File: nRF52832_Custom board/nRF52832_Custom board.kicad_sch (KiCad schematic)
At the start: 46 parts, among them J1 USB_C, J2 Battery Connector, J3 Analog, J4 PO PINS, J5 PO PINS, J6 PO PINS, J7 POWER, J8 GND, J9 Programming, SW1 SW_Push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

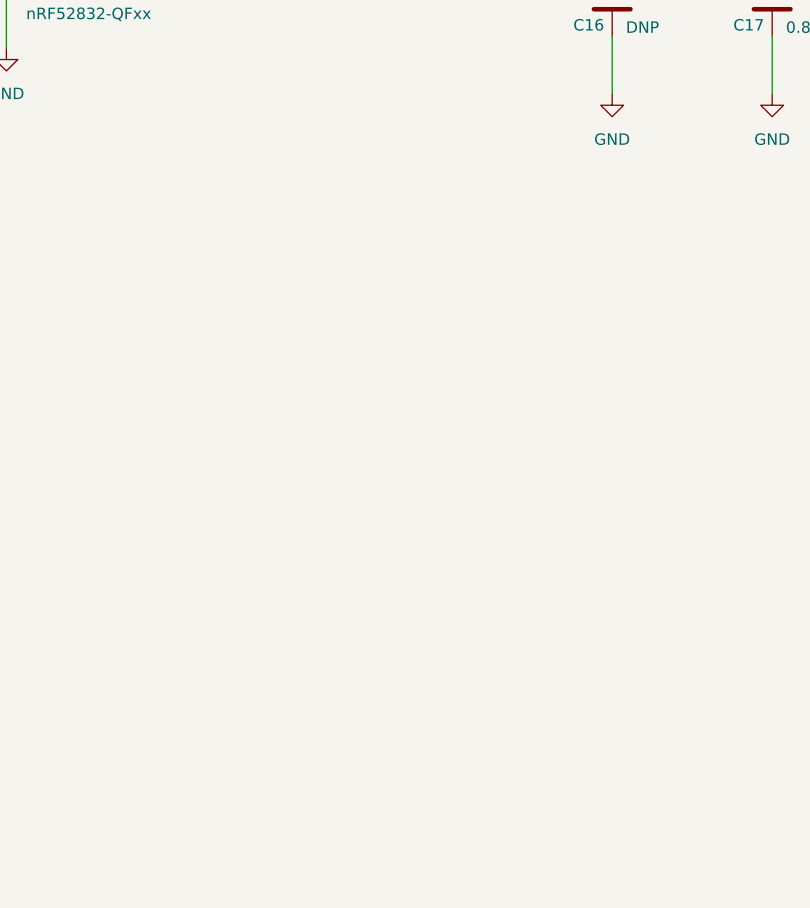
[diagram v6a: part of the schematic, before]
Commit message: update i2C and SPI
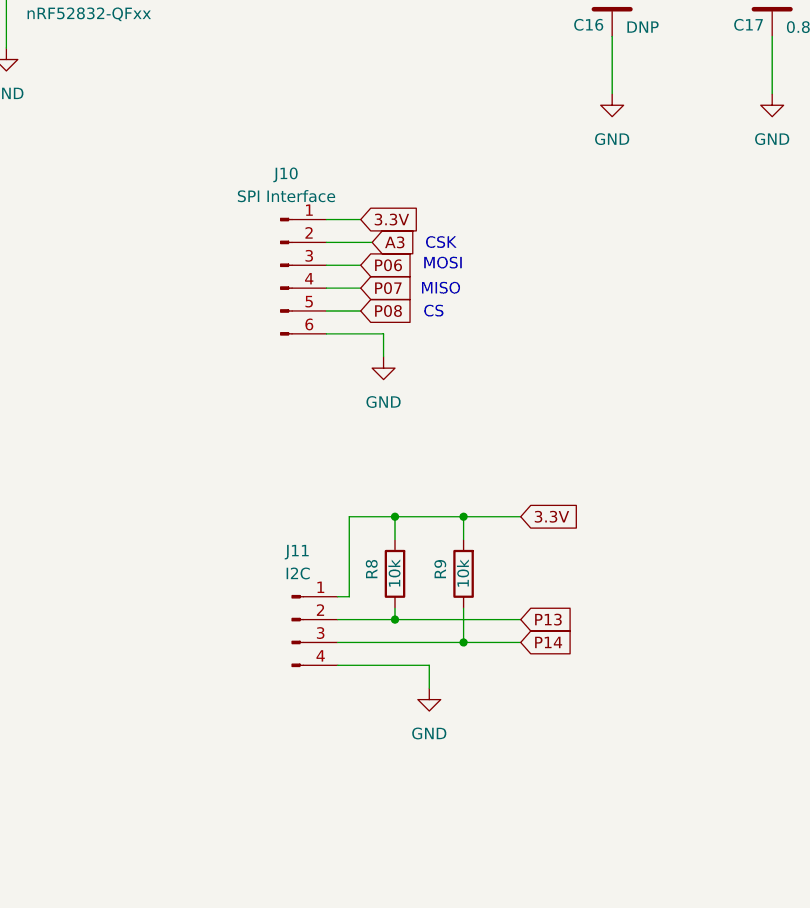
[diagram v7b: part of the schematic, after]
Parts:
- added J10: SPI Interface, Connector_JST:JST_XA_B06B-XASK-1_1x06_P2.50mm_Vertical, symbol Connector:Conn_01x06_Pin
- added J11: I2C, Connector_JST:JST_EH_B4B-EH-A_1x04_P2.50mm_Vertical, symbol Connector:Conn_01x04_Pin
- added R8, R9: 10k, Resistor_SMD:R_1206_3216Metric_Pad1.30x1.75mm_HandSolder, symbol Device:R
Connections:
- net 3.3V: now also J10.1 (Pin_1), J11.1 (Pin_1), R8.2, R9.2
- net A3: now also J10.2 (Pin_2)
- net GND: now also J10.6 (Pin_6), J11.4 (Pin_4)
- net P06: now also J10.3 (Pin_3)
- net P07: now also J10.4 (Pin_4)
- net P08: now also J10.5 (Pin_5)
- net P13: now also J11.2 (Pin_2), R8.1
- net P14: now also J11.3 (Pin_3), R9.1
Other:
- note added: "CS"
- note added: "CSK"
- note added: "MISO"
- note added: "MOSI"

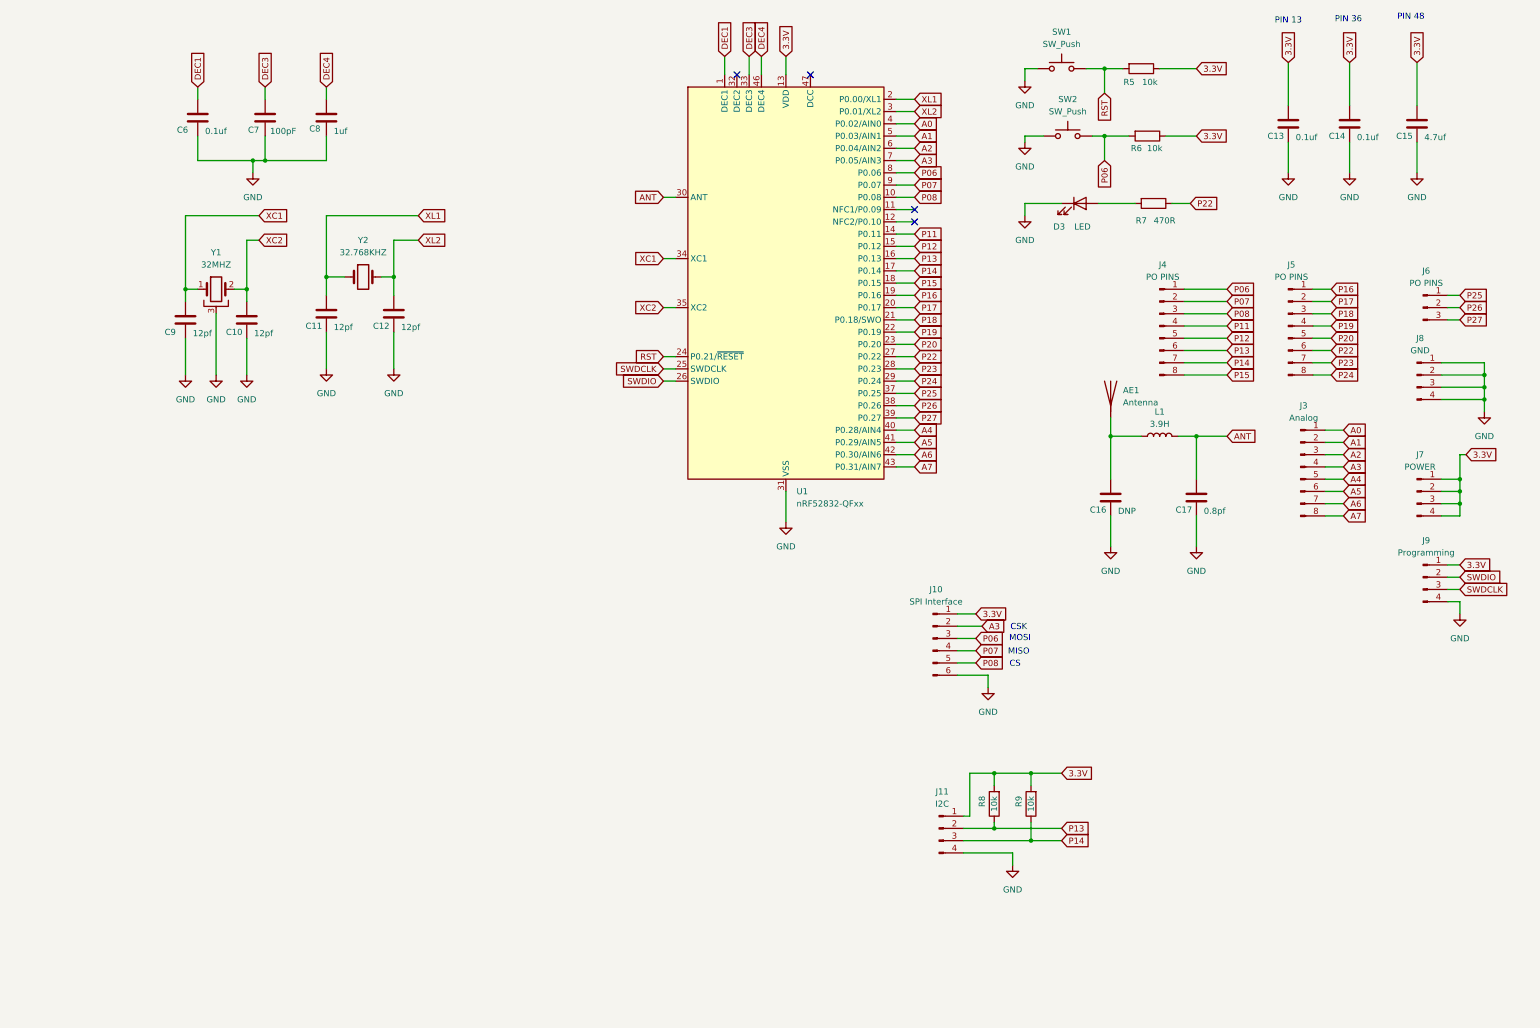
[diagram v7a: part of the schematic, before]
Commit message: DRV,Antenna Foot Print
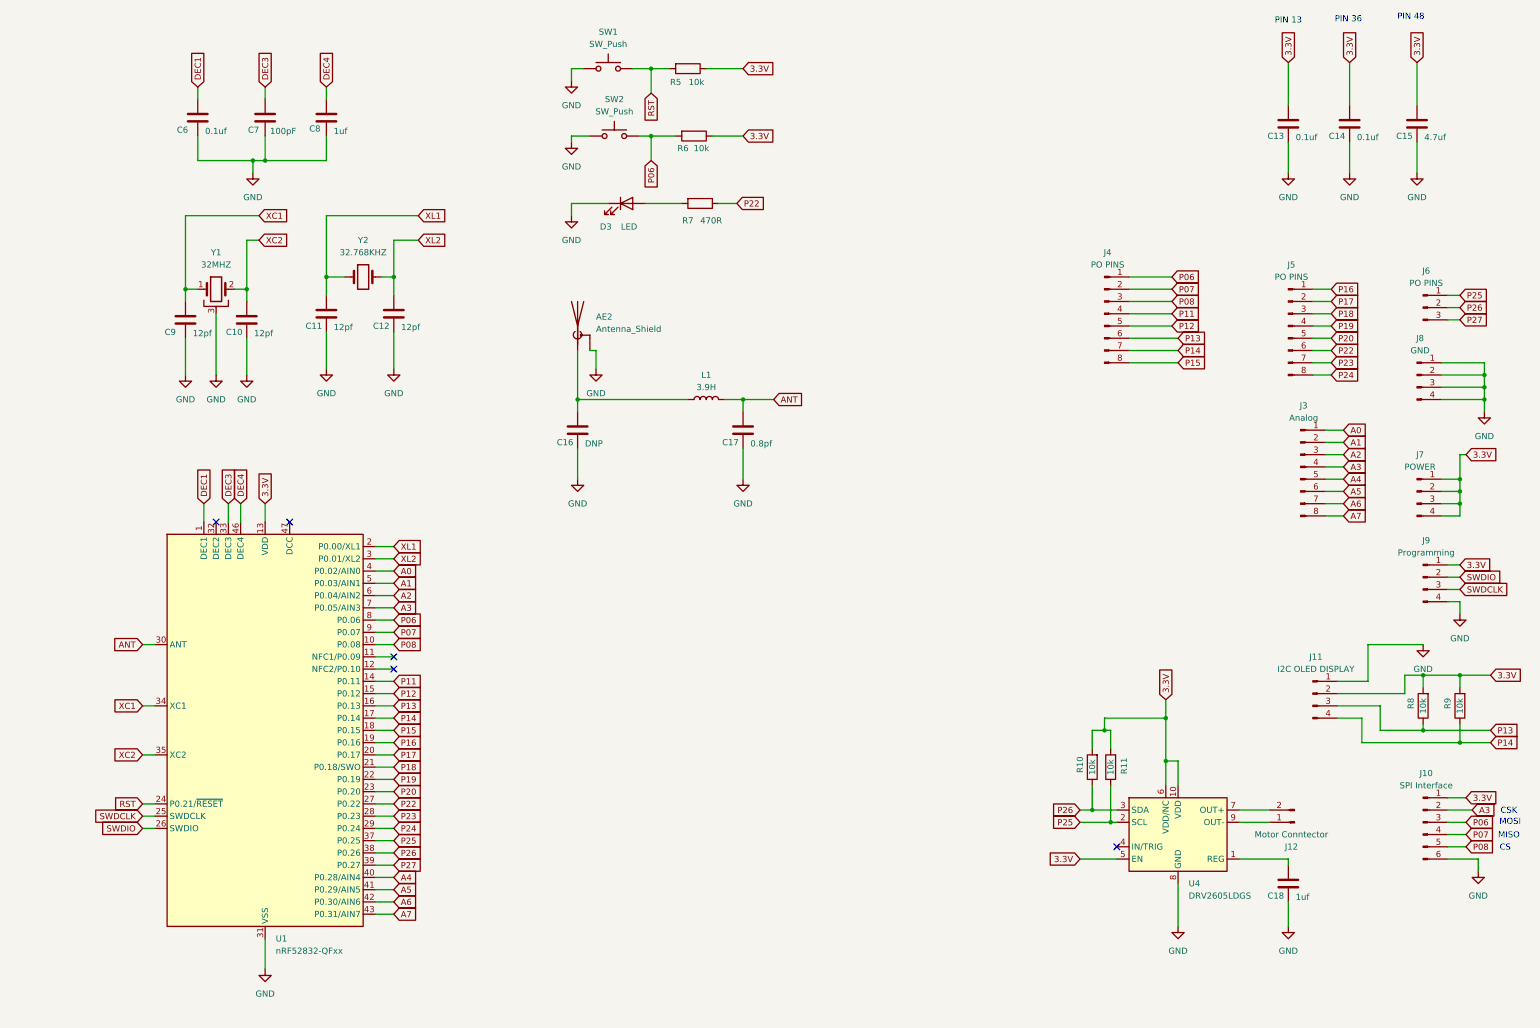
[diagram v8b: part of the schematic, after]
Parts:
- removed AE1: Antenna, RF_Antenna:Texas_SWRA117D_2.4GHz_Right, symbol Device:Antenna
- added AE2: Antenna_Shield, RF_Antenna:Texas_SWRA117D_2.4GHz_Right, symbol Device:Antenna_Shield
- added C18: 1uf, Capacitor_SMD:C_1206_3216Metric_Pad1.33x1.80mm_HandSolder, symbol Device:C
- added J12: Motor Conntector, Connector_JST:JST_XA_B02B-XASK-1_1x02_P2.50mm_Vertical, symbol Connector:Conn_01x02_Pin
- added R10, R11: 10k, Resistor_SMD:R_1206_3216Metric_Pad1.30x1.75mm_HandSolder, symbol Device:R
- added U4: DRV2605LDGS, Package_SO:VSSOP-10_3x3mm_P0.5mm, symbol Driver_Haptic:DRV2605LDGS
- J11: value I2C -> I2C OLED DISPLAY
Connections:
- net 3.3V: now also J11.2 (Pin_2), R10.2, R11.2, U4.10 (VDD), U4.5 (EN), U4.6 (VDD/NC); no longer J11.1 (Pin_1)
- net GND: now also J11.1 (Pin_1), AE2.2 (Shield), C18.2, U4.8 (GND); no longer J11.4 (Pin_4)
- net P13: now also J11.3 (Pin_3); no longer J11.2 (Pin_2)
- net P14: now also J11.4 (Pin_4); no longer J11.3 (Pin_3)
- net P25: now also R11.1, U4.2 (SCL)
- net P26: now also R10.1, U4.3 (SDA)
- net at C16.1, L1.1: now also AE2.1 (A)
- new net: C18.1, U4.1 (REG)
- new net: J12.2 (Pin_2), U4.7 (OUT+)
- new net: J12.1 (Pin_1), U4.9 (OUT-)
- no-connect marks 10 -> 11
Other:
- moved on the sheet: C16, C17, D3, J10, J11, J4, L1, R5, R6, R7, R8, R9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
